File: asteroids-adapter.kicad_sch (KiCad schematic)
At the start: 15 parts, among them J1 Asteroids PCB connector, J2 Asteroids harness connector, U1 TL074

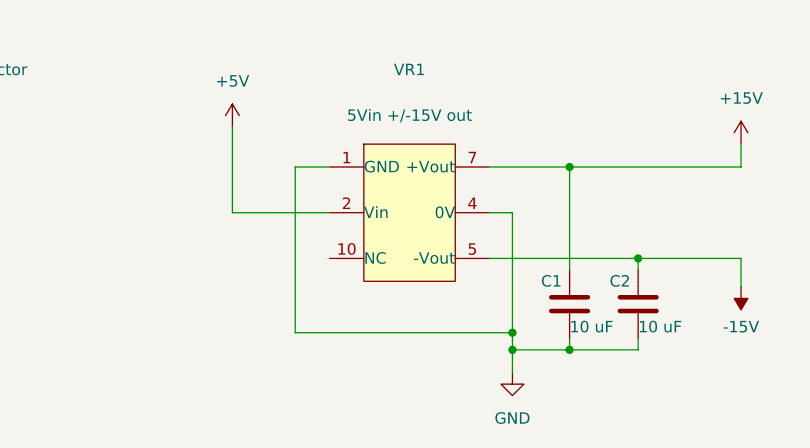
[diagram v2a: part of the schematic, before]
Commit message: Replace SMT DC/DC converter with Through-hole Part
Retro hobbyists prefer through hole.
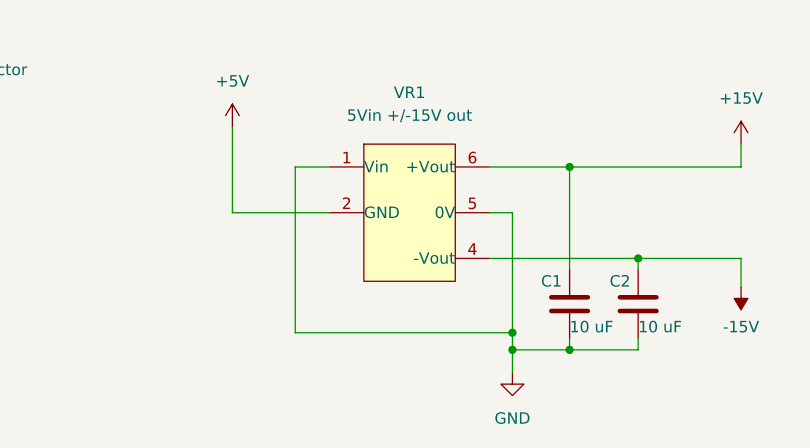
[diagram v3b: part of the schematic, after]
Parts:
- removed VR1: CUI PESE1-S5-D15-M, asteroids-adapter:CONV_PESE1-S5-D15-M, symbol ast-adapter:CUI PESE1-S5-D15-M
- added VR1: CUI PDM1-S5-D15-S, asteroids-adapter:CONV_PDM1-S5-D15-S, symbol ast-adapter:CUI PDM1-S5-D15-S
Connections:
- net +15V: now also VR1.6 (+Vout)
- net +5V: now also VR1.2 (GND)
- net -15V: now also VR1.4 (-Vout)
- net GND: now also VR1.1 (Vin), VR1.5 (0V)
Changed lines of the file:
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@@
     (pin "Z")
-  )
-  (symbol (lib_id "ast-adapter:CUI PESE1-S5-D15-M") (at 151.765 34.925 0) (unit 1)
-    (in_bom yes) (on_board yes) (fields_autoplaced)
-    (property "Reference" "VR1" (id 0) (at 151.765 19.05 0))
-    (property "Value" "CUI PESE1-S5-D15-M" (id 1) (at 126.365 140.843 0)
-      (effects (font (size 1.27 1.27)) (justify left) hide)
-    )
-    (property "Footprint" "asteroids-adapter:CONV_PESE1-S5-D15-M" (id 2) (at 151.765 21.59 0)
-      (effects (font (size 1.27 1.27)) hide)
-    )
-    (property "Datasheet" "https://www.google.com/url?sa=t&rct=j&q=&esrc=s&source=web&cd=&ved=2ahUKEwikiImr1v71AhUpk2oFHTgCD7YQFnoECAsQAQ&url=https%3A%2F%2Fwww.cui.com%2Fproduct%2Fresource%2Fpese1-m.pdf&usg=AOvVaw32_tGXML3NiDlAvSu1C1ul" (id 3) (at 128.143 135.509 0)
-      (effects (font (size 1.27 1.27)) hide)
-    )
-    (property "Component Value" "5Vin +/-15V out" (id 4) (at 151.765 24.13 0))
-    (property "Tolerance" "" (id 5) (at 132.207 145.669 0)
-      (effects (font (size 1.27 1.27)) hide)
-    )
-    (property "Manufacturer" "CUI" (id 6) (at 128.143 124.333 0)
-      (effects (font (size 1.27 1.27)) hide)
-    )
-    (property "Manufacturer Link" "https://www.cui.com/product/dc-dc-converters/isolated/pese1-m-series" (id 7) (at 130.937 130.937 0)
-      (effects (font (size 1.27 1.27)) hide)
-    )
-    (property "RoHS Document Link" "https://www.cui.com/product/resource/material-compliance/pese1-m-series" (id 8) (at 131.191 170.815 0)
-      (effects (font (size 1.27 1.27)) hide)
-    )
-    (property "Manufacturer PN" "PESE1-5S-D12-M" (id 9) (at 130.429 127.889 0)
-      (effects (font (size 1.27 1.27)) hide)
-    )
-    (property "RoHS" "Yes" (id 10) (at 127.889 168.021 0)
-      (effects (font (size 1.27 1.27)) hide)
-    )
-    (property "Allow Substitution" "No" (id 11) (at 127.635 173.863 0)
-      (effects (font (size 1.27 1.27)) hide)
-    )
-    (property "Fitted" "Yes" (id 12) (at 128.651 178.689 0)
-      (effects (font (size 1.27 1.27)) hide)
-    )
-    (property "Tracking" "No" (id 13) (at 128.143 176.149 0)
-      (effects (font (size 1.27 1.27)) hide)
-    )
-    (property "BOM Comment" "" (id 14) (at 154.305 106.045 0)
-      (effects (font (size 1.27 1.27)) hide)
-    )
-    (property "Component Type" "DC-DC converter" (id 15) (at 149.733 142.875 0)
-      (effects (font (size 1.27 1.27)) hide)
-    )
-    (property "Package Type" "SMT" (id 16) (at 116.205 121.285 0)
-      (effects (font (size 1.27 1.27)) hide)
-    )
-    (property "Package Variant" "" (id 17) (at 154.305 106.045 0)
-      (effects (font (size 1.27 1.27)) hide)
-    )
-    (property "Number of Pins" "If applicable" (id 18) (at 132.207 148.209 0)
-      (effects (font (size 1.27 1.27)) hide)
-    )
-    (property "Temp (Storage)" "If applicable" (id 19) (at 132.207 150.241 0)
-      (effects (font (size 1.27 1.27)) hide)
-    )
-    (property "Temp (Operating)" "If applicable" (id 20) (at 132.461 152.781 0)
-      (effects (font (size 1.27 1.27)) hide)
-    )
-    (property "Temp (Soldering)" "If applicable" (id 21) (at 132.461 155.575 0)
-      (effects (font (size 1.27 1.27)) hide)
-    )
-    (property "Temp Coeff." "If applicable" (id 22) (at 132.461 158.115 0)
-      (effects (font (size 1.27 1.27)) hide)
-    )
-    (property "Power Rating" "If applicable" (id 23) (at 132.461 160.655 0)
-      (effects (font (size 1.27 1.27)) hide)
-    )
-    (property "Material" "If applicable" (id 24) (at 132.461 162.941 0)
-      (effects (font (size 1.27 1.27)) hide)
-    )
-    (property "Class" "If applicable" (id 25) (at 132.461 165.227 0)
-      (effects (font (size 1.27 1.27)) hide)
-    )
-    (property "Standards Version" "1.1" (id 26) (at 128.651 181.737 0)
-      (effects (font (size 1.27 1.27)) hide)
-    )
-    (pin "1")
-    (pin "10")
-    (pin "2")
-    (pin "4")
-    (pin "5")
-    (pin "7")
   )
   (symbol (lib_id "ast-adapter:Yageo 10K ohm 1% thin film TH") (at 170.815 83.82 0) (unit 1)
@@
     (pin "1")
   )
+  (symbol (lib_id "ast-adapter:CUI  PDM1-S5-D15-S") (at 151.765 34.925 0) (unit 1)
+    (in_bom yes) (on_board yes) (fields_autoplaced)
+    (property "Reference" "VR1" (id 0) (at 151.765 21.59 0))
+    (property "Value" "CUI  PDM1-S5-D15-S" (id 1) (at 126.365 140.843 0)
+      (effects (font (size 1.27 1.27)) (justify left) hide)
+    )
+    (property "Footprint" "asteroids-adapter:CONV_PDM1-S5-D15-S" (id 2) (at 141.224 49.022 0)
+      (effects (font (size 1.27 1.27)) hide)
+    )
+    (property "Datasheet" "https://www.cui.com/product/resource/pdf/pdm1-s.pdf" (id 3) (at 128.143 135.509 0)
+      (effects (font (size 1.27 1.27)) hide)
+    )
+    (property "Component Value" "5Vin +/-15V out" (id 4) (at 151.765 24.13 0))
+    (property "Tolerance" "" (id 5) (at 132.207 145.669 0)
+      (effects (font (size 1.27 1.27)) hide)
+    )
+    (property "Manufacturer" "CUI" (id 6) (at 128.143 124.333 0)
+      (effects (font (size 1.27 1.27)) hide)
+    )
+    (property "Manufacturer Link" "https://www.cui.com/product/dc-dc-converters/isolated/pdm1-s-series" (id 7) (at 130.937 130.937 0)
+      (effects (font (size 1.27 1.27)) hide)
+    )
+    (property "RoHS Document Link" "https://www.cui.com/product/resource/material-compliance/pdm1-s-series" (id 8) (at 131.191 170.815 0)
+      (effects (font (size 1.27 1.27)) hide)
+    )
+    (property "Manufacturer PN" " PDM1-S5-D15-S" (id 9) (at 130.429 127.889 0)
+      (effects (font (size 1.27 1.27)) hide)
+    )
+    (property "RoHS" "Yes" (id 10) (at 127.889 168.021 0)
+      (effects (font (size 1.27 1.27)) hide)
+    )
+    (property "Allow Substitution" "No" (id 11) (at 127.635 173.863 0)
+      (effects (font (size 1.27 1.27)) hide)
+    )
+    (property "Fitted" "Yes" (id 12) (at 128.651 178.689 0)
+      (effects (font (size 1.27 1.27)) hide)
+    )
+    (property "Tracking" "No" (id 13) (at 128.143 176.149 0)
+      (effects (font (size 1.27 1.27)) hide)
+    )
+    (property "BOM Comment" "" (id 14) (at 154.305 106.045 0)
+      (effects (font (size 1.27 1.27)) hide)
+    )
+    (property "Component Type" "DC-DC converter" (id 15) (at 149.733 142.875 0)
+      (effects (font (size 1.27 1.27)) hide)
+    )
+    (property "Package Type" "Through Hole" (id 16) (at 116.205 121.285 0)
+      (effects (font (size 1.27 1.27)) hide)
+    )
+    (property "Package Variant" "" (id 17) (at 154.305 106.045 0)
+      (effects (font (size 1.27 1.27)) hide)
+    )
+    (property "Number of Pins" "If applicable" (id 18) (at 132.207 148.209 0)
+      (effects (font (size 1.27 1.27)) hide)
+    )
+    (property "Temp (Storage)" "If applicable" (id 19) (at 132.207 150.241 0)
+      (effects (font (size 1.27 1.27)) hide)
+    )
+    (property "Temp (Operating)" "If applicable" (id 20) (at 132.461 152.781 0)
+      (effects (font (size 1.27 1.27)) hide)
+    )
+    (property "Temp (Soldering)" "If applicable" (id 21) (at 132.461 155.575 0)
+      (effects (font (size 1.27 1.27)) hide)
+    )
+    (property "Temp Coeff." "If applicable" (id 22) (at 132.461 158.115 0)
+      (effects (font (size 1.27 1.27)) hide)
+    )
+    (property "Power Rating" "If applicable" (id 23) (at 132.461 160.655 0)
+      (effects (font (size 1.27 1.27)) hide)
+    )
+    (property "Material" "If applicable" (id 24) (at 132.461 162.941 0)
+      (effects (font (size 1.27 1.27)) hide)
+    )
+    (property "Class" "If applicable" (id 25) (at 132.461 165.227 0)
+      (effects (font (size 1.27 1.27)) hide)
+    )
+    (property "Standards Version" "1.1" (id 26) (at 128.651 181.737 0)
+      (effects (font (size 1.27 1.27)) hide)
+    )
+    (pin "1")
+    (pin "2")
+    (pin "4")
+    (pin "5")
+    (pin "6")
+  )
   (symbol (lib_id "ast-adapter:Yageo 10K ohm 1% thin film TH") (at 177.165 132.715 0) (unit 1)
     (in_bom yes) (on_board yes)
@@
       (reference "U1") (unit 5) (value "TL074") (footprint "Package_DIP:DIP-14_W7.62mm_LongPads")
     )
-    (path "/ac8d8548-4df8-4c39-8021-1ae8f0fd4c70"
-      (reference "VR1") (unit 1) (value "CUI PESE1-S5-D15-M") (footprint "asteroids-adapter:CONV_PESE1-S5-D15-M")
-    )
-  )
+    (path "/fafdd477-a3b3-411d-9d57-1c296ebf1344"
+      (reference "VR1") (unit 1) (value "CUI  PDM1-S5-D15-S") (footprint "asteroids-adapter:CONV_PDM1-S5-D15-S")
+    )
+  )
